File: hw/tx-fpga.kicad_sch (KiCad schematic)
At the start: 12 parts, among them U1101 ICE40UP3K-UWG30ITR1K

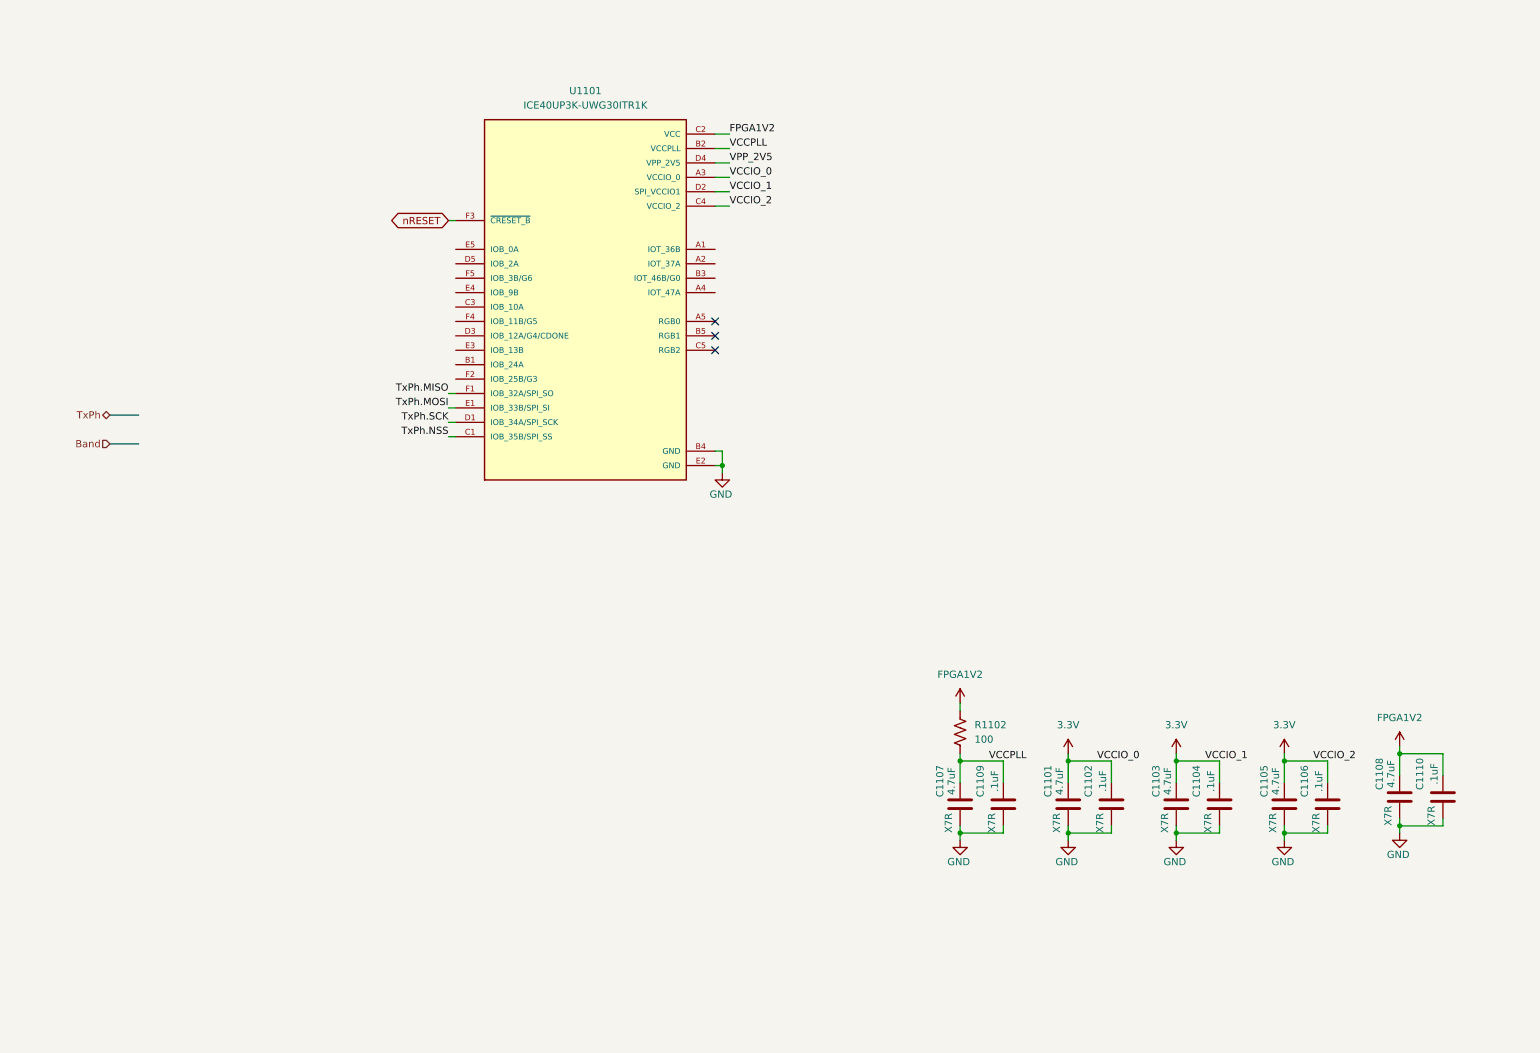
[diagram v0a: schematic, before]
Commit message: Tx LPF and its selection is pretty much done. Fix some OCD. Start to describe the design and construction.
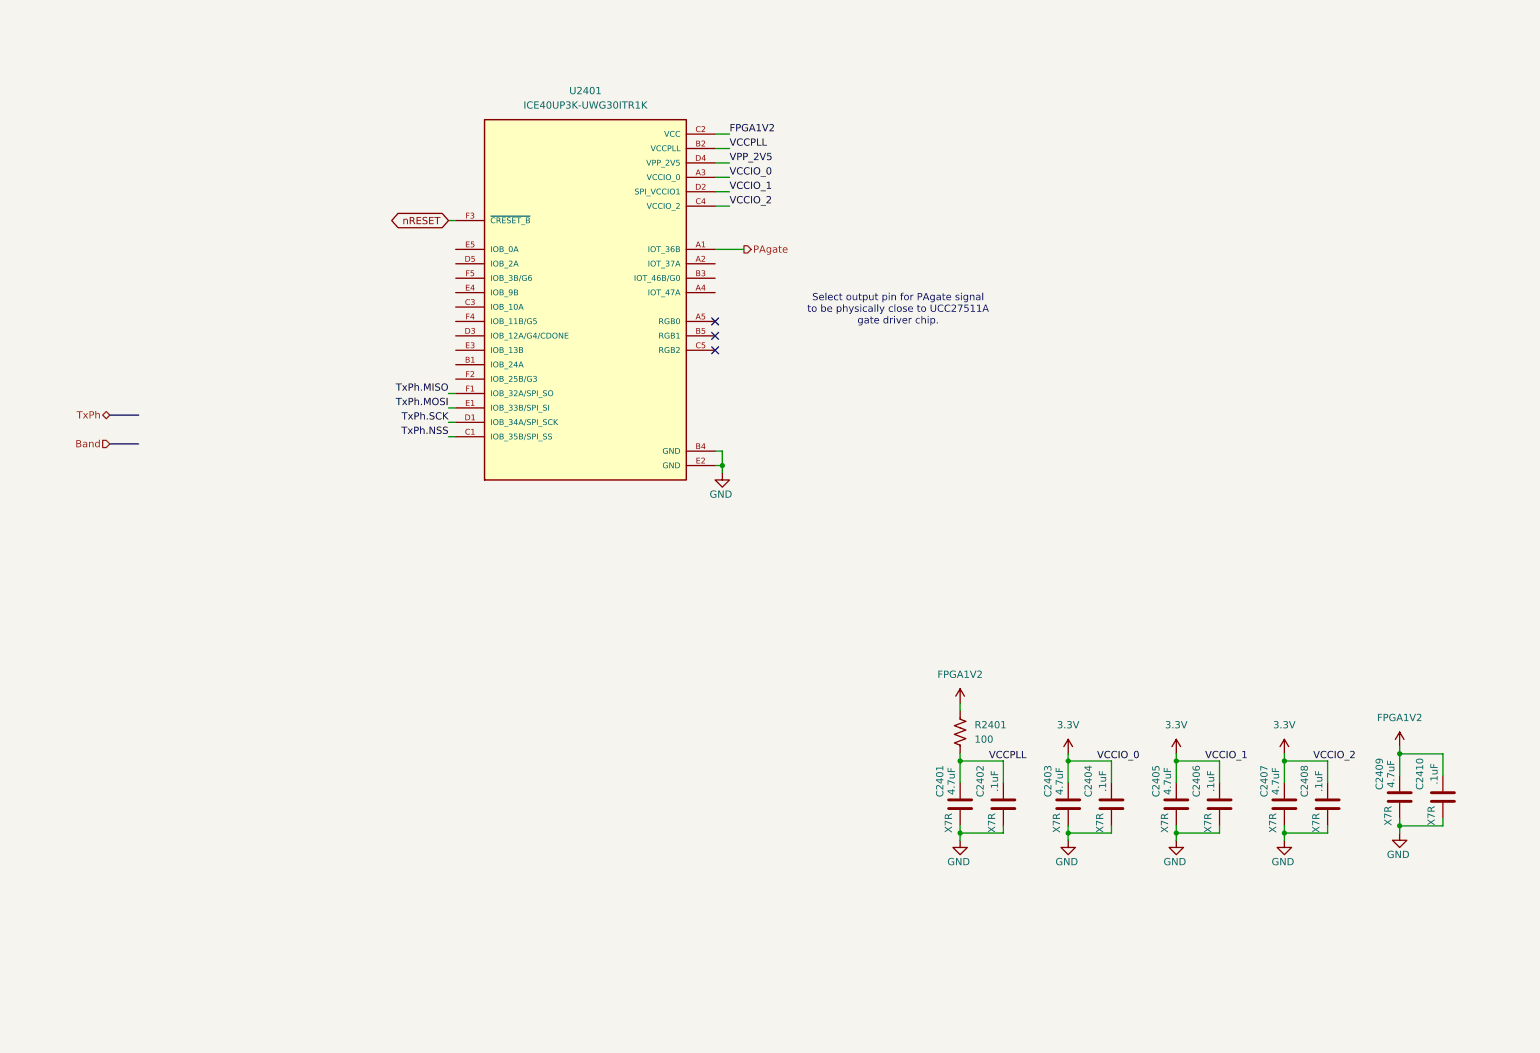
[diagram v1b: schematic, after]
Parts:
- renumbered C1107 to C2401, C1109 to C2402, C1101 to C2403, C1102 to C2404, C1103 to C2405, C1104 to C2406, C1105 to C2407, C1106 to C2408, C1108 to C2409, C1110 to C2410, R1102 to R2401, U1101 to U2401
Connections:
- net PAgate: now reaches U2401.A1 (IOT_36B)
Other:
- note added: "Select output pin for PAgate signal to be physically close to UCC27511A gate driver chip."
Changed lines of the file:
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@@
 	(generator_version "9.0")
 	(paper "A4")
+	(text "Select output pin for PAgate signal\nto be physically close to UCC27511A\ngate driver chip."
+		(exclude_from_sim no)
+		(at 171.958 66.548 0)
+		(effects
+			(font
+				(size 1.27 1.27)
+			)
+		)
+	)
 	(junction
 		(at 260.35 144.78)
@@
 		(pts
 			(xy 182.88 149.86) (xy 182.88 146.05)
+		)
+		(stroke
+			(width 0)
+			(type default)
+		)
+	)
+	(wire
+		(pts
+			(xy 139.7 55.88) (xy 144.78 55.88)
 		)
 		(stroke
@@
 				(hide yes)
 			)
+		)
+	)
+	(hierarchical_label "PAgate"
+		(shape output)
+		(at 144.78 55.88 0)
+		(effects
+			(font
+				(size 1.27 1.27)
+			)
+			(justify left)
 		)
 	)
@@
 		(on_board yes)
 		(dnp no)
-		(property "Reference" "C1106"
+		(property "Reference" "C2408"
 			(at 243.586 149.606 90)
 			(effects
@@
 			(project "USB-SSB-txcvr"
 				(path "/8ae46c04-d01a-4756-8774-512b694bfaff/2406d03c-531b-4eaf-8b4b-4b266b9d0f2b/068cc90c-d1ce-4b82-ba62-fdba2623f1f6"
-					(reference "C1106")
+					(reference "C2408")
 					(unit 1)
 				)
@@
 		(on_board yes)
 		(dnp no)
-		(property "Reference" "C1104"
+		(property "Reference" "C2406"
 			(at 224.536 149.606 90)
 			(effects
@@
 			(project "USB-SSB-txcvr"
 				(path "/8ae46c04-d01a-4756-8774-512b694bfaff/2406d03c-531b-4eaf-8b4b-4b266b9d0f2b/068cc90c-d1ce-4b82-ba62-fdba2623f1f6"
-					(reference "C1104")
+					(reference "C2406")
 					(unit 1)
 				)
@@
 		(on_board yes)
 		(dnp no)
-		(property "Reference" "#PWR01102"
+		(property "Reference" "#PWR02405"
 			(at 201.93 166.37 0)
 			(effects
@@
 			(project "USB-SSB-txcvr"
 				(path "/8ae46c04-d01a-4756-8774-512b694bfaff/2406d03c-531b-4eaf-8b4b-4b266b9d0f2b/068cc90c-d1ce-4b82-ba62-fdba2623f1f6"
-					(reference "#PWR01102")
+					(reference "#PWR02405")
 					(unit 1)
 				)
@@
 		(on_board yes)
 		(dnp no)
-		(property "Reference" "C1105"
+		(property "Reference" "C2407"
 			(at 236.474 149.606 90)
 			(effects
@@
 			(project "USB-SSB-txcvr"
 				(path "/8ae46c04-d01a-4756-8774-512b694bfaff/2406d03c-531b-4eaf-8b4b-4b266b9d0f2b/068cc90c-d1ce-4b82-ba62-fdba2623f1f6"
-					(reference "C1105")
+					(reference "C2407")
 					(unit 1)
 				)
@@
 		(on_board yes)
 		(dnp no)
-		(property "Reference" "C1109"
+		(property "Reference" "C2402"
 			(at 186.436 149.606 90)
 			(effects
@@
 			(project "USB-SSB-txcvr"
 				(path "/8ae46c04-d01a-4756-8774-512b694bfaff/2406d03c-531b-4eaf-8b4b-4b266b9d0f2b/068cc90c-d1ce-4b82-ba62-fdba2623f1f6"
-					(reference "C1109")
+					(reference "C2402")
 					(unit 1)
 				)
@@
 		(on_board yes)
 		(dnp no)
-		(property "Reference" "C1107"
+		(property "Reference" "C2401"
 			(at 179.324 149.606 90)
 			(effects
@@
 			(project "USB-SSB-txcvr"
 				(path "/8ae46c04-d01a-4756-8774-512b694bfaff/2406d03c-531b-4eaf-8b4b-4b266b9d0f2b/068cc90c-d1ce-4b82-ba62-fdba2623f1f6"
-					(reference "C1107")
+					(reference "C2401")
 					(unit 1)
 				)
@@
 		(on_board yes)
 		(dnp no)
-		(property "Reference" "#PWR01111"
+		(property "Reference" "#PWR02411"
 			(at 260.35 165.1 0)
 			(effects
@@
 			(project "USB-SSB-txcvr"
 				(path "/8ae46c04-d01a-4756-8774-512b694bfaff/2406d03c-531b-4eaf-8b4b-4b266b9d0f2b/068cc90c-d1ce-4b82-ba62-fdba2623f1f6"
-					(reference "#PWR01111")
+					(reference "#PWR02411")
 					(unit 1)
 				)
@@
 		(on_board yes)
 		(dnp no)
-		(property "Reference" "#PWR01109"
+		(property "Reference" "#PWR02403"
 			(at 182.88 166.37 0)
 			(effects
@@
 			(project "USB-SSB-txcvr"
 				(path "/8ae46c04-d01a-4756-8774-512b694bfaff/2406d03c-531b-4eaf-8b4b-4b266b9d0f2b/068cc90c-d1ce-4b82-ba62-fdba2623f1f6"
-					(reference "#PWR01109")
+					(reference "#PWR02403")
 					(unit 1)
 				)
@@
 		(on_board yes)
 		(dnp no)
-		(property "Reference" "#PWR01110"
+		(property "Reference" "#PWR02410"
 			(at 260.35 147.32 0)
 			(effects
@@
 			(project "USB-SSB-txcvr"
 				(path "/8ae46c04-d01a-4756-8774-512b694bfaff/2406d03c-531b-4eaf-8b4b-4b266b9d0f2b/068cc90c-d1ce-4b82-ba62-fdba2623f1f6"
-					(reference "#PWR01110")
+					(reference "#PWR02410")
 					(unit 1)
 				)
@@
 		(dnp no)
 		(fields_autoplaced yes)
-		(property "Reference" "U1101"
+		(property "Reference" "U2401"
 			(at 116.84 27.94 0)
 			(effects
@@
 			(project "USB-SSB-txcvr"
 				(path "/8ae46c04-d01a-4756-8774-512b694bfaff/2406d03c-531b-4eaf-8b4b-4b266b9d0f2b/068cc90c-d1ce-4b82-ba62-fdba2623f1f6"
-					(reference "U1101")
+					(reference "U2401")
 					(unit 1)
 				)
@@
 		(on_board yes)
 		(dnp no)
-		(property "Reference" "C1101"
+		(property "Reference" "C2403"
 			(at 198.374 149.606 90)
 			(effects
@@
 			(project "USB-SSB-txcvr"
 				(path "/8ae46c04-d01a-4756-8774-512b694bfaff/2406d03c-531b-4eaf-8b4b-4b266b9d0f2b/068cc90c-d1ce-4b82-ba62-fdba2623f1f6"
-					(reference "C1101")
+					(reference "C2403")
 					(unit 1)
 				)
@@
 		(on_board yes)
 		(dnp no)
-		(property "Reference" "C1110"
+		(property "Reference" "C2410"
 			(at 263.906 148.336 90)
 			(effects
@@
 			(project "USB-SSB-txcvr"
 				(path "/8ae46c04-d01a-4756-8774-512b694bfaff/2406d03c-531b-4eaf-8b4b-4b266b9d0f2b/068cc90c-d1ce-4b82-ba62-fdba2623f1f6"
-					(reference "C1110")
+					(reference "C2410")
 					(unit 1)
 				)
@@
 		(on_board yes)
 		(dnp no)
-		(property "Reference" "C1108"
+		(property "Reference" "C2409"
 			(at 256.794 148.336 90)
 			(effects
@@
 			(project "USB-SSB-txcvr"
 				(path "/8ae46c04-d01a-4756-8774-512b694bfaff/2406d03c-531b-4eaf-8b4b-4b266b9d0f2b/068cc90c-d1ce-4b82-ba62-fdba2623f1f6"
-					(reference "C1108")
+					(reference "C2409")
 					(unit 1)
 				)
@@
 		(on_board yes)
 		(dnp no)
-		(property "Reference" "C1102"
+		(property "Reference" "C2404"
 			(at 205.486 149.606 90)
 			(effects
@@
 			(project "USB-SSB-txcvr"
 				(path "/8ae46c04-d01a-4756-8774-512b694bfaff/2406d03c-531b-4eaf-8b4b-4b266b9d0f2b/068cc90c-d1ce-4b82-ba62-fdba2623f1f6"
-					(reference "C1102")
+					(reference "C2404")
 					(unit 1)
 				)
@@
 		(dnp no)
 		(fields_autoplaced yes)
-		(property "Reference" "#PWR01108"
+		(property "Reference" "#PWR02402"
 			(at 182.88 139.7 0)
 			(effects
@@
 			(project "USB-SSB-txcvr"
 				(path "/8ae46c04-d01a-4756-8774-512b694bfaff/2406d03c-531b-4eaf-8b4b-4b266b9d0f2b/068cc90c-d1ce-4b82-ba62-fdba2623f1f6"
-					(reference "#PWR01108")
+					(reference "#PWR02402")
 					(unit 1)
 				)
@@
 		(dnp no)
 		(fields_autoplaced yes)
-		(property "Reference" "R1102"
+		(property "Reference" "R2401"
 			(at 185.42 139.6999 0)
 			(effects
@@
 			(project "USB-SSB-txcvr"
 				(path "/8ae46c04-d01a-4756-8774-512b694bfaff/2406d03c-531b-4eaf-8b4b-4b266b9d0f2b/068cc90c-d1ce-4b82-ba62-fdba2623f1f6"
-					(reference "R1102")
+					(reference "R2401")
 					(unit 1)
 				)
@@
 		(dnp no)
 		(fields_autoplaced yes)
-		(property "Reference" "#PWR01106"
+		(property "Reference" "#PWR02408"
 			(at 240.03 148.59 0)
 			(effects
@@
 			(project "USB-SSB-txcvr"
 				(path "/8ae46c04-d01a-4756-8774-512b694bfaff/2406d03c-531b-4eaf-8b4b-4b266b9d0f2b/068cc90c-d1ce-4b82-ba62-fdba2623f1f6"
-					(reference "#PWR01106")
+					(reference "#PWR02408")
 					(unit 1)
 				)
@@
 		(dnp no)
 		(fields_autoplaced yes)
-		(property "Reference" "#PWR01101"
+		(property "Reference" "#PWR02404"
 			(at 201.93 148.59 0)
 			(effects
@@
 			(project "USB-SSB-txcvr"
 				(path "/8ae46c04-d01a-4756-8774-512b694bfaff/2406d03c-531b-4eaf-8b4b-4b266b9d0f2b/068cc90c-d1ce-4b82-ba62-fdba2623f1f6"
-					(reference "#PWR01101")
+					(reference "#PWR02404")
 					(unit 1)
 				)
@@
 		(on_board yes)
 		(dnp no)
-		(property "Reference" "C1103"
+		(property "Reference" "C2405"
 			(at 217.424 149.606 90)
 			(effects
@@
 			(project "USB-SSB-txcvr"
 				(path "/8ae46c04-d01a-4756-8774-512b694bfaff/2406d03c-531b-4eaf-8b4b-4b266b9d0f2b/068cc90c-d1ce-4b82-ba62-fdba2623f1f6"
-					(reference "C1103")
+					(reference "C2405")
 					(unit 1)
 				)
@@
 		(on_board yes)
 		(dnp no)
-		(property "Reference" "#PWR01107"
+		(property "Reference" "#PWR02409"
 			(at 240.03 166.37 0)
 			(effects
@@
 			(project "USB-SSB-txcvr"
 				(path "/8ae46c04-d01a-4756-8774-512b694bfaff/2406d03c-531b-4eaf-8b4b-4b266b9d0f2b/068cc90c-d1ce-4b82-ba62-fdba2623f1f6"
-					(reference "#PWR01107")
+					(reference "#PWR02409")
 					(unit 1)
 				)
@@
 		(on_board yes)
 		(dnp no)
-		(property "Reference" "#PWR01105"
+		(property "Reference" "#PWR02401"
 			(at 140.97 101.6 0)
 			(effects
@@
 			(project "USB-SSB-txcvr"
 				(path "/8ae46c04-d01a-4756-8774-512b694bfaff/2406d03c-531b-4eaf-8b4b-4b266b9d0f2b/068cc90c-d1ce-4b82-ba62-fdba2623f1f6"
-					(reference "#PWR01105")
+					(reference "#PWR02401")
 					(unit 1)
 				)
@@
 		(on_board yes)
 		(dnp no)
-		(property "Reference" "#PWR01104"
+		(property "Reference" "#PWR02407"
 			(at 220.98 166.37 0)
 			(effects
@@
 			(project "USB-SSB-txcvr"
 				(path "/8ae46c04-d01a-4756-8774-512b694bfaff/2406d03c-531b-4eaf-8b4b-4b266b9d0f2b/068cc90c-d1ce-4b82-ba62-fdba2623f1f6"
-					(reference "#PWR01104")
+					(reference "#PWR02407")
 					(unit 1)
 				)
@@
 		(dnp no)
 		(fields_autoplaced yes)
-		(property "Reference" "#PWR01103"
+		(property "Reference" "#PWR02406"
 			(at 220.98 148.59 0)
 			(effects
@@
 			(project "USB-SSB-txcvr"
 				(path "/8ae46c04-d01a-4756-8774-512b694bfaff/2406d03c-531b-4eaf-8b4b-4b266b9d0f2b/068cc90c-d1ce-4b82-ba62-fdba2623f1f6"
-					(reference "#PWR01103")
+					(reference "#PWR02406")
 					(unit 1)
 				)

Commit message: Checkpoint
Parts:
- removed U2401: ICE40UP3K-UWG30ITR1K, ICE40UP3K-UWG30ITR1K:BGA30N40P6X5_253X211X60N, symbol ICE40UP3K-UWG30ITR1K:ICE40UP3K-UWG30ITR1K
- added C2424: 0.1uF, symbol Device:C
- added C2425: 1uF, symbol Device:C
- added U2402: ICE40UP5K-SG48ITR, Package_DFN_QFN:QFN-48-1EP_7x7mm_P0.5mm_EP5.6x5.6mm, symbol FPGA_Lattice:ICE40UP5K-SG48ITR
- added Y2401: FT2MNTUM-30.0-T1, FT2MNTUM300T1, symbol FT2MNTUM-30.0-T1:FT2MNTUM-30.0-T1
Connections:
- net 3.3V: now also U2402.1 (VCCIO_2), U2402.22 (SPI_VCCIO1), U2402.33 (VCCIO_0)
- net FPGA1V2: now also U2402.30 (VCC), U2402.5 (VCC)
- net GND: now also C2424.2, C2425.2, U2402.49 (GND), Y2401.1 (GND_1), Y2401.2 (GND_2)
- net PAgate: now also U2402.25 (IOT_36b)
- net TxPh.MISO: now also U2402.14 (IOB_32a_SPI_SO)
- net TxPh.MOSI: now also U2402.17 (IOB_33b_SPI_SI)
- net TxPh.NSS: now also U2402.16 (IOB_35b_SPI_SS)
- net TxPh.SCK: now also U2402.15 (IOB_34a_SPI_SCK)
- net VPP_2V5: now also U2402.24 (VPP_2V5)
- net nRESET: now also U2402.8 (~{CRESET})
- net VCCPLL: no longer names the net of C2401.1, C2402.1, R2401.2
- net VCCPLL: now also U2402.29 (VCCPLL)
- new net: U2402.44 (IOB_3b_G6), Y2401.3 (OUTPUT)
- new net +3.3V: C2424.1, C2425.1, Y2401.4 (VDD)
- new net RxPh0: U2402.6 (IOB_13b)
- new net RxPh1: U2402.9 (IOB_16a)
- new net STM32clock: U2402.10 (IOB_18a)
- no-connect marks 3 -> 1
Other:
- note added: "Schmitt triggered"
- moved on the sheet: C2401, C2402, C2403, C2404, C2405, C2406, C2407, C2408, C2409, C2410, R2401

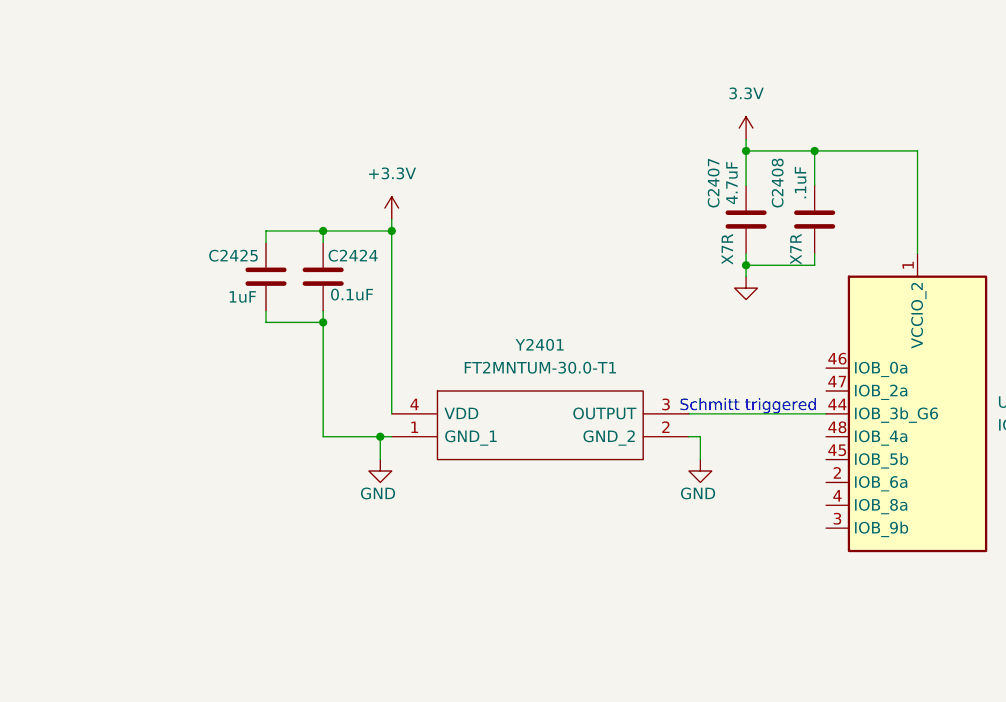
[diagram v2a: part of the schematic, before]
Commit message: FPGA package changed to 48-pin QFP. Starting FPGA power sequencing. Set up 40MHz HCMOS TCXO.
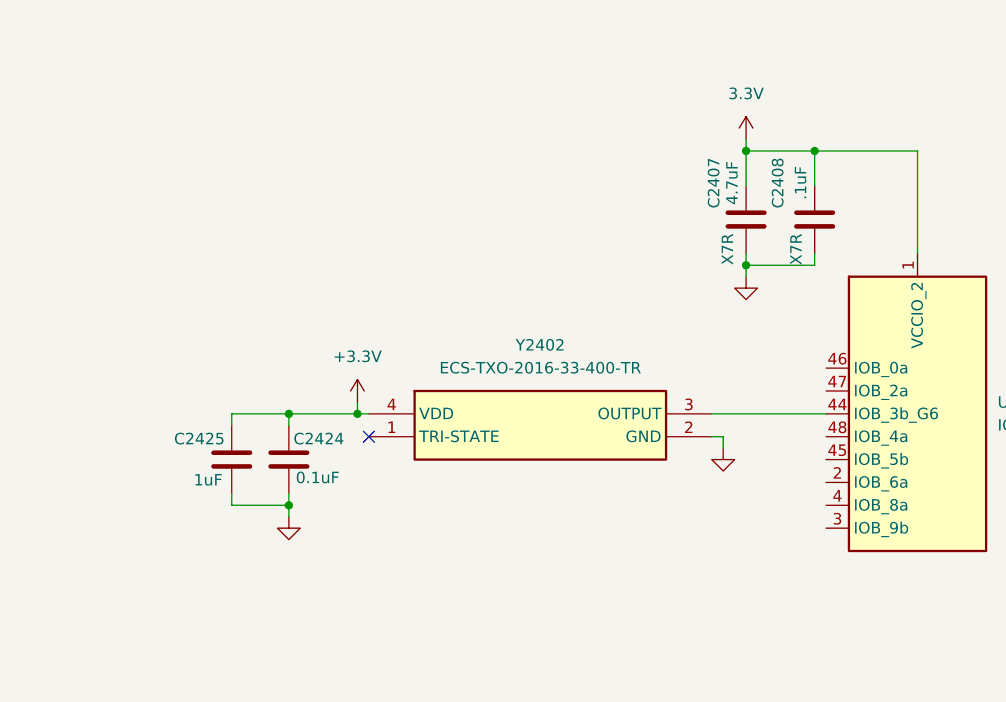
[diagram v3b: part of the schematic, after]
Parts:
- removed Y2401: FT2MNTUM-30.0-T1, FT2MNTUM300T1, symbol FT2MNTUM-30.0-T1:FT2MNTUM-30.0-T1
- added Y2402: ECS-TXO-2016-33-400-TR, ECSTXO201633400TR, symbol ECS-TXO-2016-33-400-TR:ECS-TXO-2016-33-400-TR
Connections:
- net +3.3V: now also Y2402.4 (VDD)
- net GND: now also Y2402.2 (GND)
- net at U2402.44 (IOB_3b_G6): now also Y2402.3 (OUTPUT)
- no-connect marks 1 -> 2
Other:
- note removed: "Schmitt triggered"
- moved on the sheet: C2424, C2425
